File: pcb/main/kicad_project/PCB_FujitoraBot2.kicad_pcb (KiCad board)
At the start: 2 copper layers, 95.6 x 100 mm, 100 parts, among them IC1 AS5040, IC2 AS5040, J1 MORRO1, SW1 SW_Push, SW2 SW_Push, SW3 SW_Push, SW4 SW_Reset, U1 MPU-6500, U2 LM1117MP-3.3, Y1 Crystal

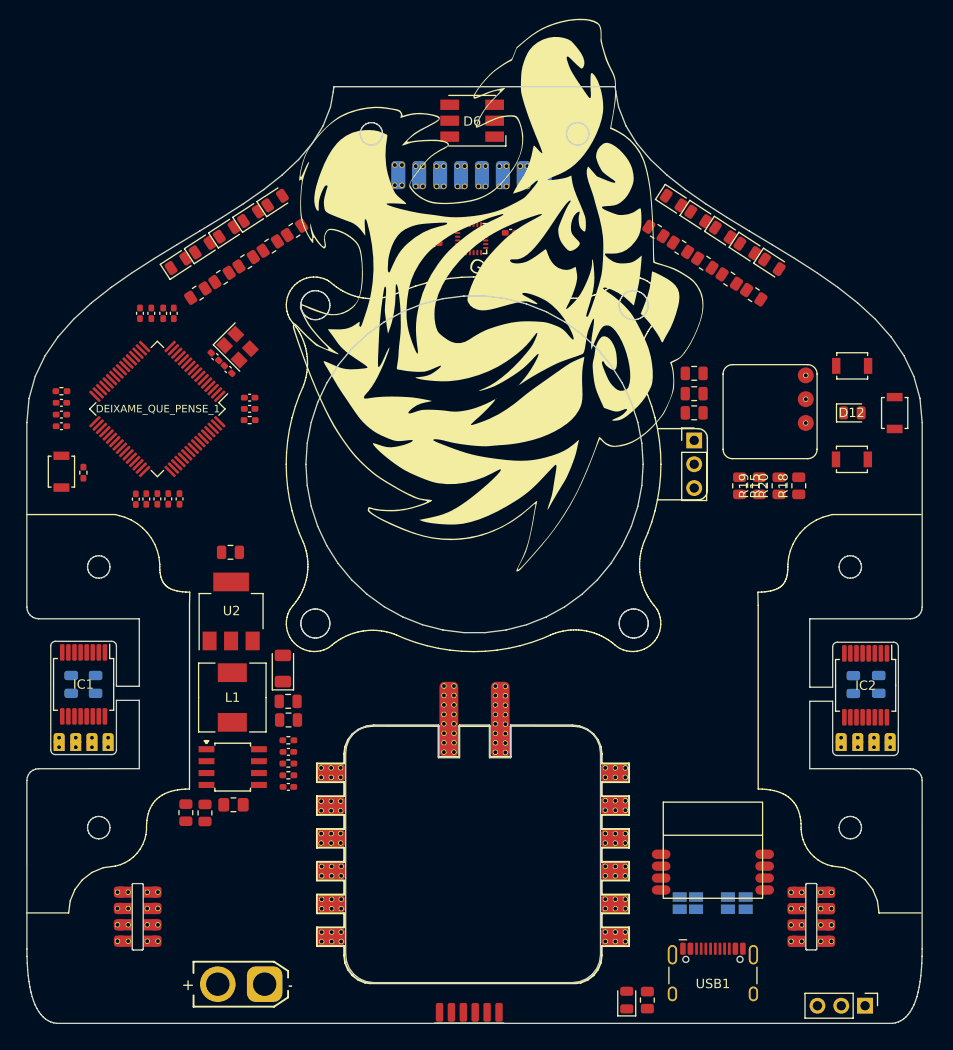
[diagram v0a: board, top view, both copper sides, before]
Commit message: Finaliza el ruteo de la PCB_main a falta de los encoders
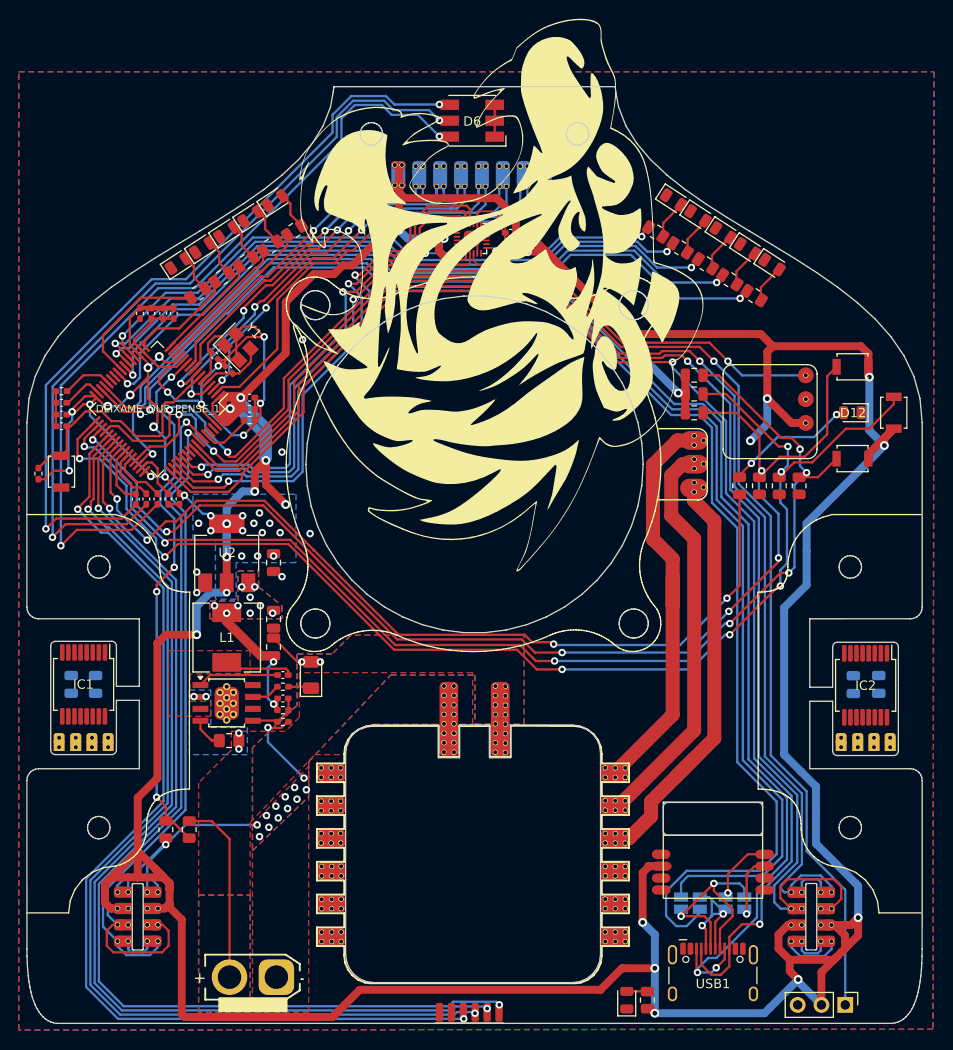
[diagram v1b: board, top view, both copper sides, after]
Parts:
- DC-DC1: footprint custom_footprints:SOP8 -> custom_footprints:SOP8_with_gnd_pad
- U1: footprint Sensor_Motion:InvenSense_QFN-24_3x3mm_P0.4mm -> custom_footprints:FujitoraBot2_giro_MPU6500
- Y1: value Crystal -> Crystal_GND24; footprint Crystal:Crystal_SMD_3225-4Pin_3.2x2.5mm -> Crystal:Crystal_SMD_TXC_7M-4Pin_3.2x2.5mm
- moved D11 12.5 mm to (180.7, 64.7)
- moved D7 12.5 mm to (170.2, 57.8)
- moved R13 12.5 mm to (178.8, 68.0)
- moved R9 12.4 mm to (168.3, 61.2)
- moved R29 9.47 mm to (128.5, 109.8)
- moved CR9 9.46 mm to (128.5, 111.0)
- moved CR7 8.90 mm to (127.5, 102.5), turned to 90 degrees
- moved CR5 8.23 mm to (128.5, 108.5), turned to 180 degrees
- moved CR8 7.96 mm to (127.5, 105.5), turned to 90 degrees
- moved DC-DC1 6.91 mm to (122.5, 111.5)
- moved CR6 6.87 mm to (122.8, 115.5)
- moved SW3 6.69 mm to (193.7, 80.5), turned to -90 degrees
- moved SW2 6.63 mm to (189.3, 85.4), turned to 0 degrees
- moved L1 6.43 mm to (122.5, 104.5)
- moved D10 6.30 mm to (178.1, 63.0)
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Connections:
- J_ESC1 pad 2: (no net) -> unconnected-(J_ESC1-Pin_2-Pad2)
- USB1 pad 11: +3V3 -> unconnected-(USB1-VBUS-Pad11)
- USB1 pad 2: +3V3 -> unconnected-(USB1-VBUS-Pad2)
- Y1 pad 2: Net-(DEIXAME_QUE_PENSE_1-PH0/OSC_IN) -> GND
- Y1 pad 3: (no net) -> Net-(DEIXAME_QUE_PENSE_1-PH0/OSC_IN)
- Y1 pad 4: (no net) -> GND
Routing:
- net +3V3: track 0.00 -> 558.4 mm, vias 0 -> 48
- net /SWDIO: track 0.00 -> 158.6 mm, vias 0 -> 3
- net /AUX: track 0.00 -> 156.3 mm, vias 0 -> 3
- net GND: track 0.00 -> 155.9 mm, vias 0 -> 30
- net Net-(DEIXAME_QUE_PENSE_1-PB10): track 0.00 -> 150.0 mm, vias 0 -> 1
- net /SWCLK: track 0.00 -> 147.6 mm, vias 0 -> 2
- net /ENC_2_B: track 0.00 -> 145.5 mm, vias 0 -> 1
- net Net-(DEIXAME_QUE_PENSE_1-PB11): track 0.00 -> 144.3 mm, vias 0 -> 1
- net /ENC_2_A: track 0.00 -> 142.4 mm, vias 0 -> 1
- net /MENU_ENTER: track 0.00 -> 139.9 mm, vias 0 -> 7
- net /MENU_ARRIBA: track 0.00 -> 131.7 mm, vias 0 -> 6
- net /MENU_ABAJO: track 0.00 -> 127.3 mm, vias 0 -> 7
- net /MotorD: track 0.00 -> 110.3 mm, vias 0 -> 2
- net /MotorS2: track 0.00 -> 109.6 mm, vias 0 -> 2
- net /MotorI: track 0.00 -> 109.1 mm, vias 0 -> 2
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- added copper zone on B.Cu, net +3V3
- added copper zone on B.Cu, net +5V
- added copper zone on F.Cu, net +5V
- added copper zone on B.Cu, net /BATT
- added copper zone on F.Cu, net /BATT
- added copper zone on B.Cu, net GND
- added copper zone on F.Cu, net GND
- added copper zone on F.Cu, net Net-(DC-DC1-SW)
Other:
- outline, holes or cut-outs redrawn

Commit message: Finaliza ruteo y añade etiquetas
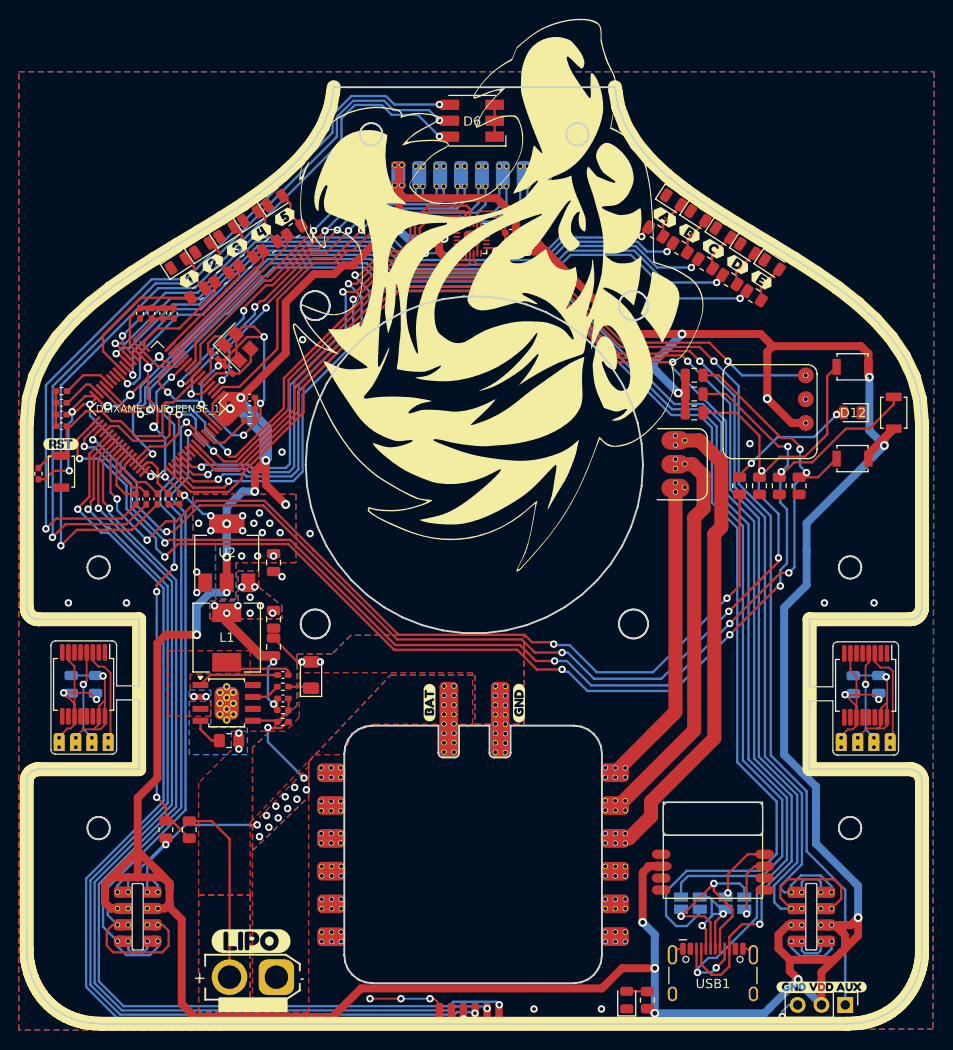
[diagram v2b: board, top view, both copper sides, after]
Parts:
- added kibuzzard-66B8D59D: G***, kibuzzard-66B8D59D, B.Cu at (176.8, 130.7)
- added kibuzzard-66B8D5B6: G***, kibuzzard-66B8D5B6, B.Cu at (172.0, 130.7)
- added kibuzzard-66B8D625: G***, kibuzzard-66B8D625, F.Cu at (153.7, 111.5)
- added kibuzzard-66B8D672: G***, kibuzzard-66B8D672, F.Cu at (125.1, 136.9)
- added kibuzzard-66B8D6B0: G***, kibuzzard-66B8D6B0, B.Cu at (149.0, 106.6)
- added kibuzzard-66B8D700: G***, kibuzzard-66B8D700, F.Cu at (186.0, 141.8)
- added kibuzzard-66B8DA7F: G***, kibuzzard-66B8DA7F, F.Cu at (144.2, 111.5)
- added kibuzzard-66B8DA98: G***, kibuzzard-66B8DA98, F.Cu at (104.8, 83.8)
- added kibuzzard-66B8DBE7: G***, kibuzzard-66B8DBE7, F.Cu at (169.3, 59.6)
- added kibuzzard-66B8DBFF: G***, kibuzzard-66B8DBFF, F.Cu at (171.9, 61.3)
- added kibuzzard-66B8DC05: G***, kibuzzard-66B8DC05, F.Cu at (174.4, 63.0)
- added kibuzzard-66B8DC0B: G***, kibuzzard-66B8DC0B, F.Cu at (177.0, 64.7)
- added kibuzzard-66B8DC13: G***, kibuzzard-66B8DC13, F.Cu at (179.6, 66.3)
- added kibuzzard-66B8DD07: G***, kibuzzard-66B8DD07, F.Cu at (121.0, 64.6)
- added kibuzzard-66B8DD11: G***, kibuzzard-66B8DD11, F.Cu at (123.6, 62.9)
- added kibuzzard-66B8DD29: G***, kibuzzard-66B8DD29, F.Cu at (118.5, 66.2)
- added kibuzzard-66B8DD65: G***, kibuzzard-66B8DD65, F.Cu at (126.2, 61.2)
- added kibuzzard-66B8DD76: G***, kibuzzard-66B8DD76, F.Cu at (128.7, 59.6)
- moved MOTOR_1 2.00 mm to (170.4, 83.5)
- turned C18 to -90 degrees
- turned C19 to -90 degrees
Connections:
- MOTOR_1 pad 1: /ESC_M1_R -> /ESC_M1_T
- MOTOR_1 pad 3: /ESC_M1_T -> /ESC_M1_R
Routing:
- net /ENC_2_GND: track 0.00 -> 18.6 mm, vias 0 -> 2
- net /ENC_1_GND: track 0.00 -> 18.5 mm, vias 0 -> 2
- net /ENC_1_3.3: track 0.00 -> 17.0 mm, vias 0 -> 1
- net /ENC_2_3.3: track 0.00 -> 16.2 mm, vias 0 -> 1
- net GND: track 155.9 -> 168.4 mm, vias 30 -> 41
- net /ENC_2_A_CONN: track 0.00 -> 10.4 mm
- net /ENC_1_A_CONN: track 0.00 -> 10.3 mm
- net /ENC_1_B_CONN: track 0.00 -> 9.63 mm, vias 0 -> 1
- net /ENC_2_B_CONN: track 0.00 -> 9.51 mm, vias 0 -> 1
- net /ESC_M1_R: track 44.8 -> 35.9 mm
- net /ESC_M1_T: track 47.0 -> 52.3 mm
- net /S_FR_X8: track 43.8 -> 40.1 mm
- net /LED_AUX: track 95.8 -> 98.2 mm
- net /MENU_ARRIBA: track 131.7 -> 134.0 mm
- net /MENU_ABAJO: track 127.3 -> 129.4 mm
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- added copper zone on F.Cu, net +3V3
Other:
- outline, holes or cut-outs redrawn
